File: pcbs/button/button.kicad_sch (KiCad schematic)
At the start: 5 parts

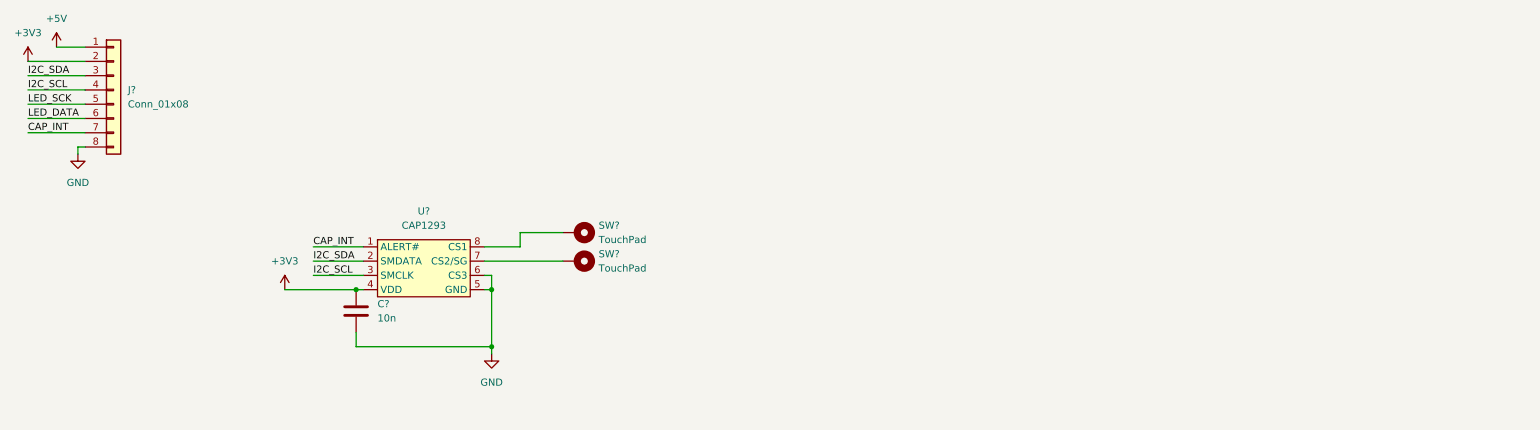
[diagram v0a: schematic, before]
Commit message: Add LEDs to button PCB.
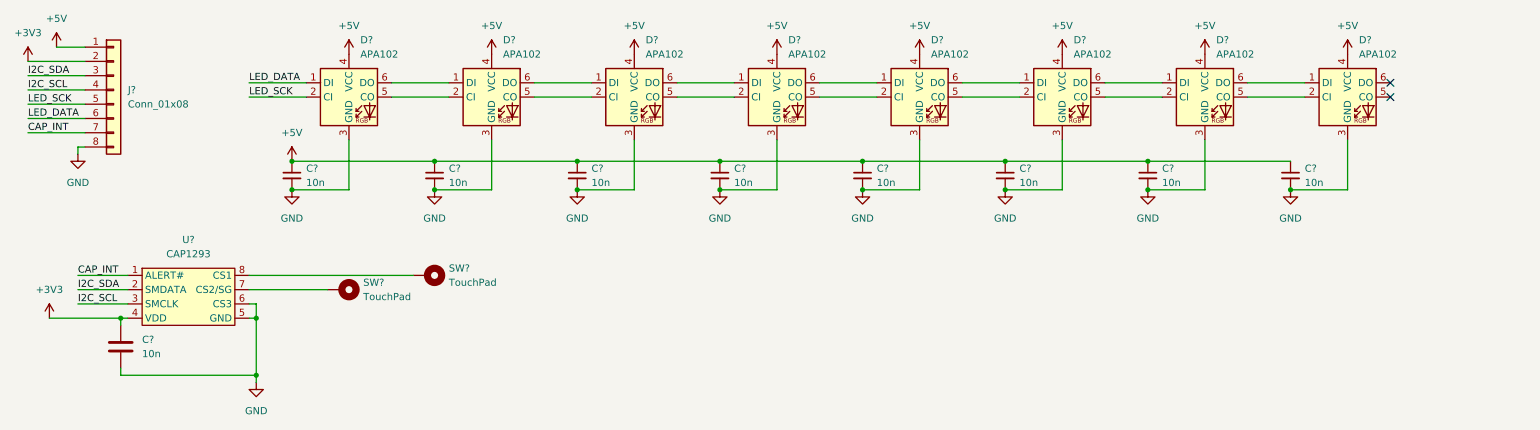
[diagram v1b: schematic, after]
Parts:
- added C? (x8): 10n, symbol Device:C_Small
- added D? (x8): APA102, LED_SMD:LED_RGB_5050-6, symbol LED:APA102
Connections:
- net +5V: now also C?.1, C?.1, C?.1, C?.1, C?.1, C?.1, C?.1, C?.1, D?.4 (VCC), D?.4 (VCC), D?.4 (VCC), D?.4 (VCC), D?.4 (VCC), D?.4 (VCC), D?.4 (VCC), D?.4 (VCC)
- net GND: now also C?.2, C?.2, C?.2, C?.2, C?.2, C?.2, C?.2, C?.2, D?.3 (GND), D?.3 (GND), D?.3 (GND), D?.3 (GND), D?.3 (GND), D?.3 (GND), D?.3 (GND), D?.3 (GND)
- net LED_DATA: now also D?.1 (DI)
- net LED_SCK: now also D?.2 (CI)
- new net: D?.1 (DI), D?.6 (DO) (x7)
- new net: D?.2 (CI), D?.5 (CO) (x7)
- no-connect marks 0 -> 2
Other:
- moved on the sheet: C?, SW?, U?

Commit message: Add PCB for capacitive button
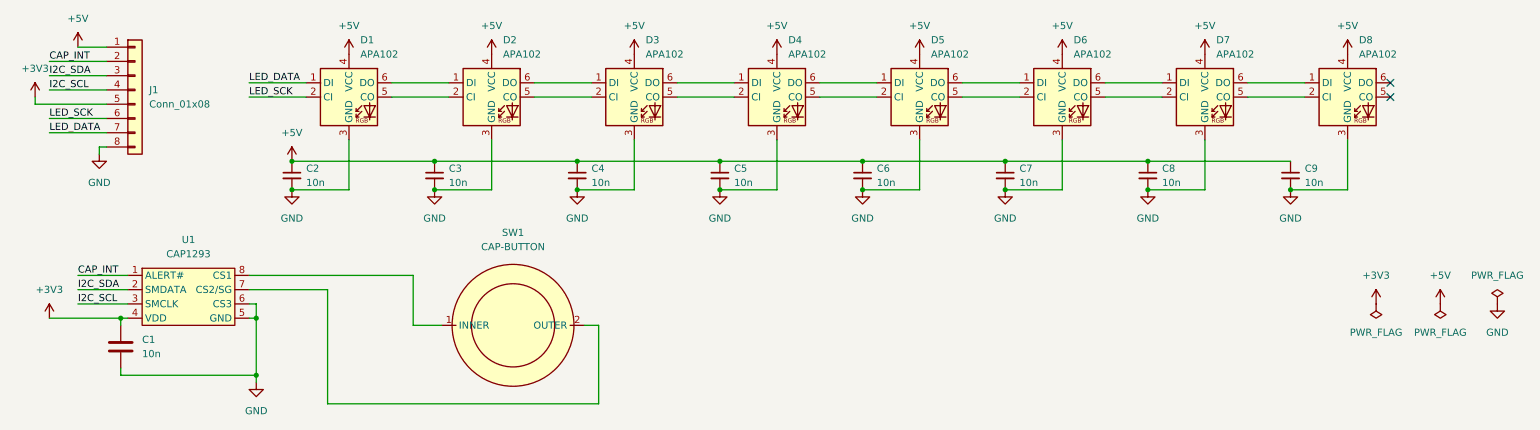
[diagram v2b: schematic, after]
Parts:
- removed SW? (x2): TouchPad, symbol Mechanical:MountingHole_Pad
- added SW1: CAP-BUTTON, touchpads:button-internal, symbol cap-button:CAP-BUTTON
- C1, C2, C3, C4, C5, C6, C7, C8, C9: renamed from C?; footprint (none) -> Capacitor_SMD:C_0805_2012Metric_Pad1.18x1.45mm_HandSolder
- D1, D2, D3, D4, D5, D6, D7, D8: renamed from D?; footprint LED_SMD:LED_RGB_5050-6 -> APA102-flipped:LED_RGB_5050-6-flipped
- J1: renamed from J?; footprint (none) -> Connector_PinHeader_2.54mm:PinHeader_1x08_P2.54mm_Vertical
- U1: renamed from U?; footprint (none) -> Package_SO:SOIC-8_3.9x4.9mm_P1.27mm
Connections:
- net +3V3: now also J1.5 (Pin_5); no longer J1.2 (Pin_2)
- net CAP_INT: now also J1.2 (Pin_2); no longer J1.7 (Pin_7)
- net LED_DATA: now also J1.7 (Pin_7); no longer J1.6 (Pin_6)
- net LED_SCK: now also J1.6 (Pin_6); no longer J1.5 (Pin_5)
- net at U1.8 (CS1): now also SW1.1 (INNER)
- net at U1.7 (CS2/SG): now also SW1.2 (OUTER)
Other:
- moved on the sheet: J1
